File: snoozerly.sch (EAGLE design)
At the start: 55 parts, among them Q1 MOSFET_PCHANNEL, Q2 MOSFET-NCHANNELFDD8780, Q3 MOSFET-NCHANNELBSS123LT1G, Q4 MOSFET-NCHANNELBSS123LT1G, U1 ATMEGA328P, Y1 32KHz, Y2 8MHz

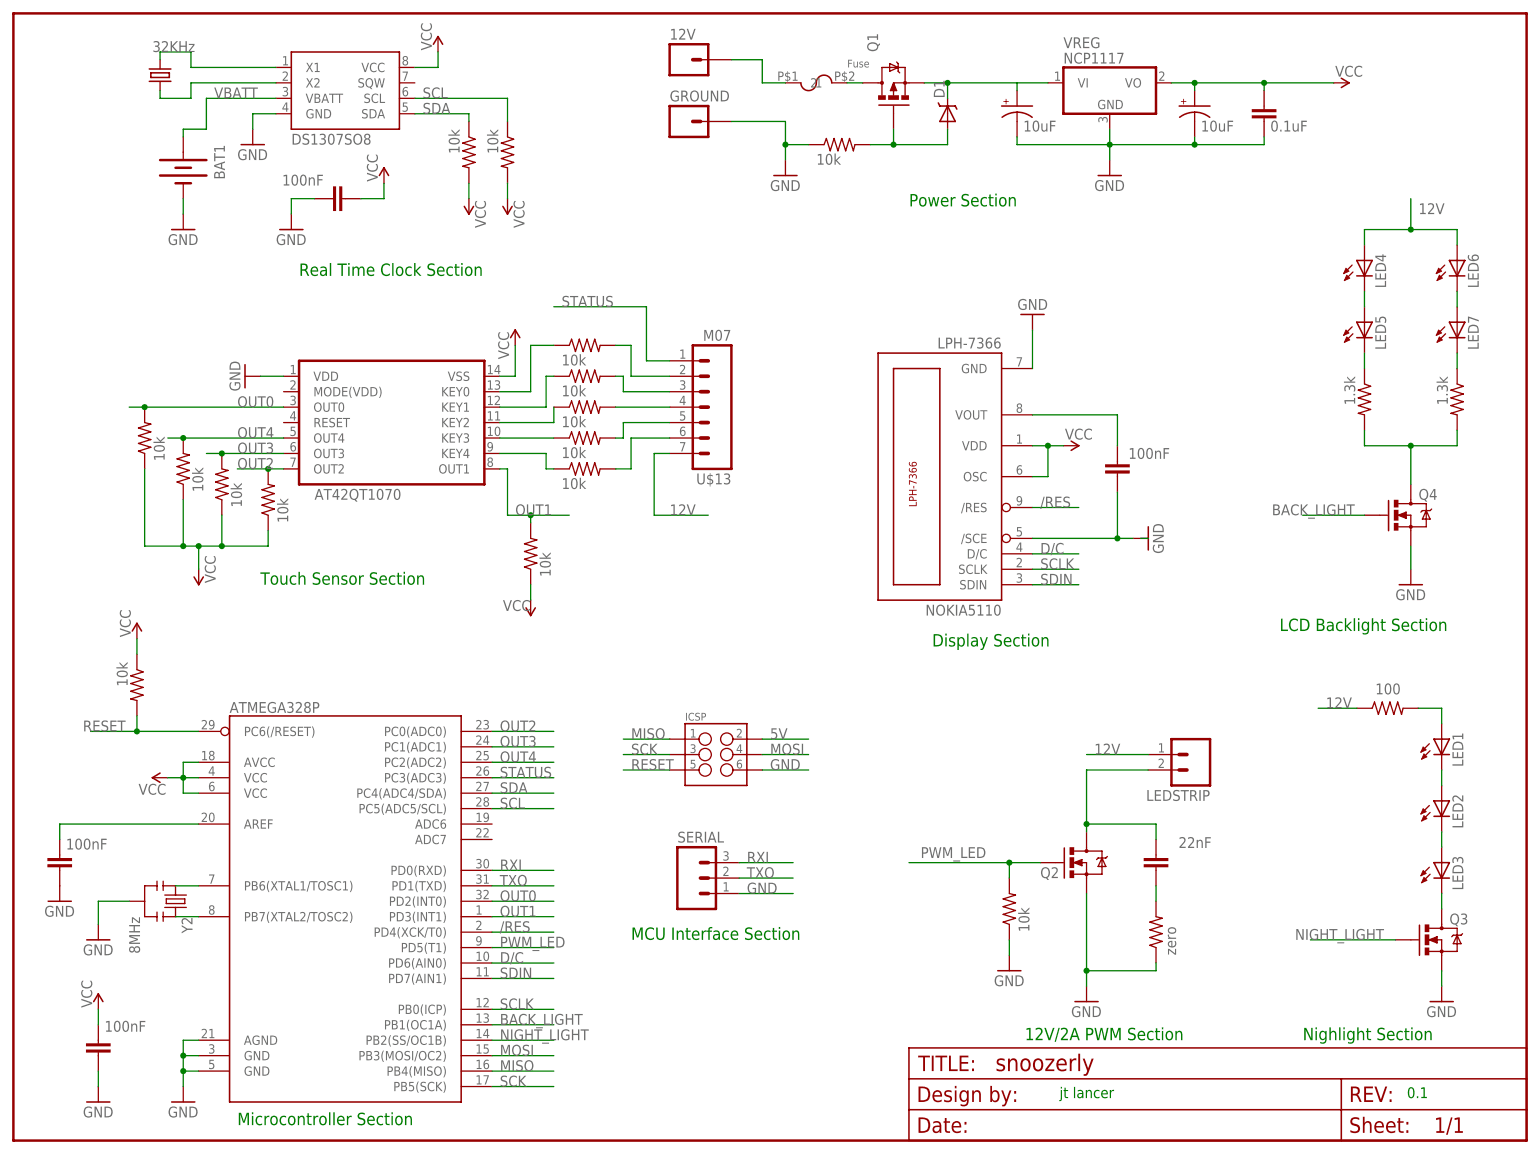
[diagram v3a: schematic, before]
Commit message: added top control board.
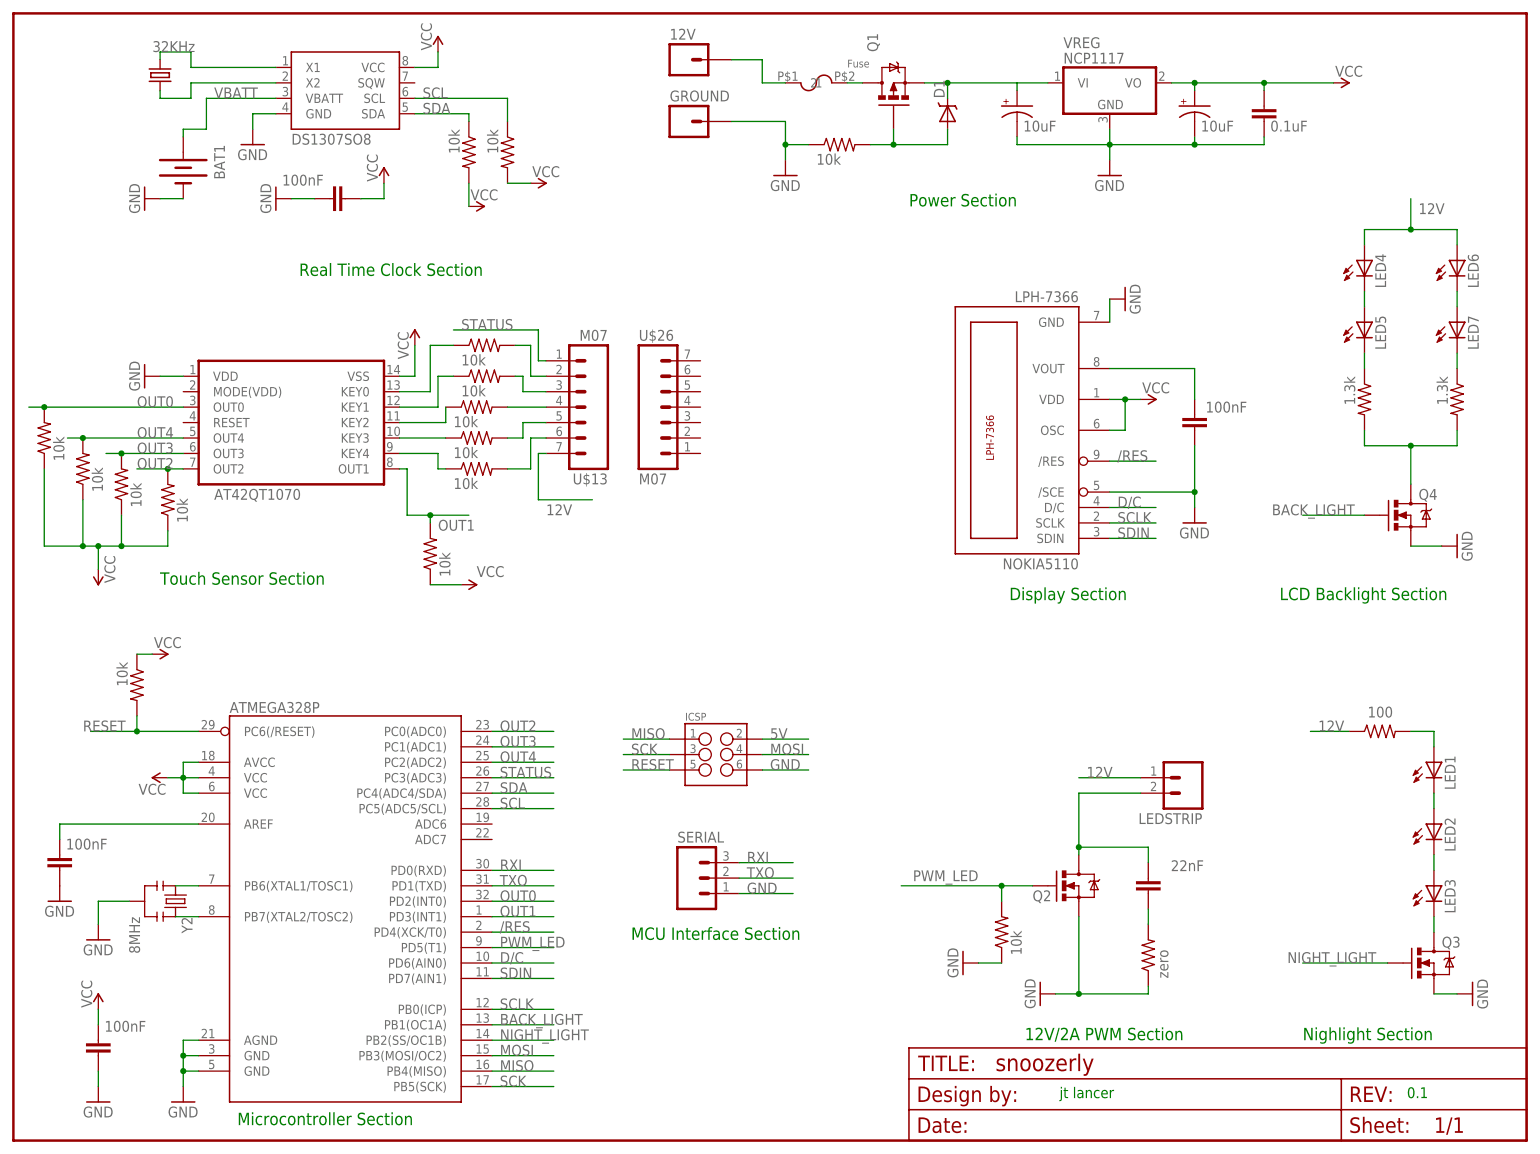
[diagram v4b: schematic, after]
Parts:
- added U$26: M07, jt_parts:M07
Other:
- moved on the sheet: LED1, LED2, LED3, LEDSTRIP, NOKIA5110, Q2, Q3, U$13

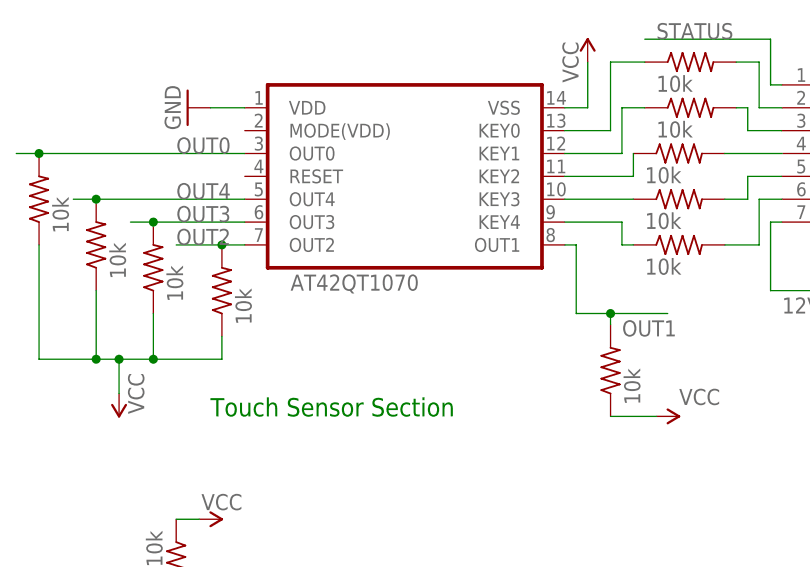
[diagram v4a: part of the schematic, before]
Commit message: updated diode and SO-14 footprint
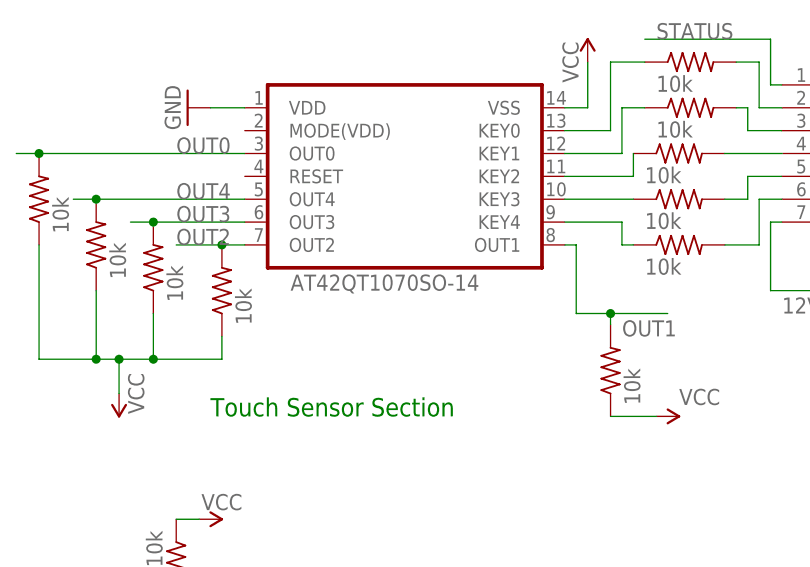
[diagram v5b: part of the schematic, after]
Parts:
- AT42QT1070: value AT42QT1070 -> AT42QT1070SO-14; device jt_parts:AT42QT1070 -> jt_parts:AT42QT1070SO-14
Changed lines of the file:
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@@
 <part name="GND1" library="SparkFun-Aesthetics" deviceset="GND" device=""/>
 <part name="U$1" library="jt_parts" deviceset="FRAME_LETTER" device=""/>
-<part name="AT42QT1070" library="jt_parts" deviceset="AT42QT1070" device=""/>
+<part name="AT42QT1070" library="jt_parts" deviceset="AT42QT1070" device="SO-14" value="AT42QT1070SO-14"/>
 <part name="SUPPLY2" library="SparkFun-Aesthetics" deviceset="VCC" device=""/>
 <part name="GND3" library="SparkFun-Aesthetics" deviceset="GND" device=""/>

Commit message: before modifying vreg footprint
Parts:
- removed U$26: M07, jt_parts:M07
- SERIAL: device SparkFun-Connectors:M03POGO_PIN_HOLES_ONLY -> SparkFun-Connectors:M031X03_NO_SILK
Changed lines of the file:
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@@
 <part name="C6" library="SparkFun-Capacitors" deviceset="CAP" device="0805" value="100nF"/>
 <part name="SUPPLY10" library="SparkFun-Aesthetics" deviceset="VCC" device=""/>
-<part name="SERIAL" library="SparkFun-Connectors" deviceset="M03" device="POGO_PIN_HOLES_ONLY"/>
+<part name="SERIAL" library="SparkFun-Connectors" deviceset="M03" device="1X03_NO_SILK"/>
 <part name="ICSP" library="SparkFun-Connectors" deviceset="M03X2" device="POGO_PINS"/>
 <part name="Q4" library="SparkFun-DiscreteSemi" deviceset="MOSFET-NCHANNEL" device="BSS123LT1G"/>
@@
 <part name="SUPPLY11" library="SparkFun-Aesthetics" deviceset="VCC" device=""/>
 <part name="U$25" library="adafruit" deviceset="R-US_" device="R0603" value="zero"/>
-<part name="U$26" library="jt_parts" deviceset="M07" device=""/>
 </parts>
 <sheets>
@@
 <attribute name="VALUE" x="205.232" y="135.89" size="1.778" layer="96" rot="R90"/>
 </instance>
-<instance part="U$26" gate="G$1" x="123.19" y="229.87"/>
 </instances>
 <busses>
@@
 </segment>
 <segment>
-<wire x1="134.62" y1="149.86" x2="143.51" y2="149.86" width="0.1524" layer="91"/>
-<pinref part="SERIAL" gate="G$1" pin="1"/>
-<label x="135.89" y="149.86" size="1.778" layer="95"/>
-</segment>
-<segment>
 <pinref part="ICSP" gate="G$1" pin="6"/>
 <wire x1="138.43" y1="170.18" x2="146.05" y2="170.18" width="0.1524" layer="91"/>
@@
 <wire x1="245.11" y1="207.01" x2="250.19" y2="207.01" width="0.1524" layer="91"/>
 </segment>
+<segment>
+<pinref part="SERIAL" gate="G$1" pin="1"/>
+<wire x1="134.62" y1="149.86" x2="143.51" y2="149.86" width="0.1524" layer="91"/>
+<label x="135.89" y="149.86" size="1.778" layer="95"/>
+</segment>
 </net>

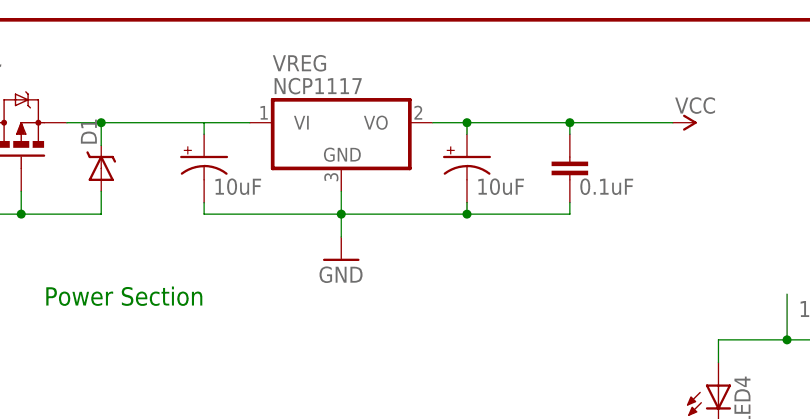
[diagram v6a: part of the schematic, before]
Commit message: updated vreg pinouts/footprint and rerouted traces
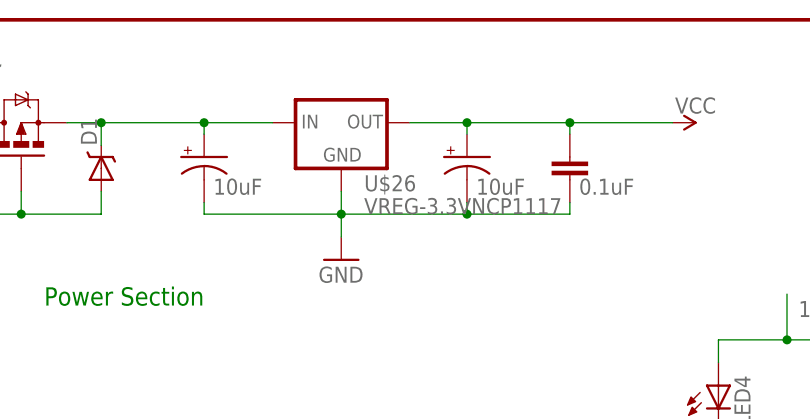
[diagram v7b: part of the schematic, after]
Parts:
- removed VREG: NCP1117, adafruit:7805DT
- added U$26: VREG-3.3VNCP1117, jt_parts:VREG-3.3VNCP1117
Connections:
- net 12V: now also U$26.IN; no longer VREG.VI
- net 5V: now also U$26.OUT; no longer VREG.VO
- net GND: now also U$26.GND; no longer VREG.GND
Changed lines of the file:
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@@
 </classes>
 <parts>
-<part name="VREG" library="adafruit" deviceset="78*" device="DT" technology="05" value="NCP1117"/>
 <part name="C8" library="SparkFun-Capacitors" deviceset="CAP" device="0805" value="0.1uF"/>
 <part name="SUPPLY3" library="SparkFun-Aesthetics" deviceset="VCC" device=""/>
@@
 <part name="SUPPLY11" library="SparkFun-Aesthetics" deviceset="VCC" device=""/>
 <part name="U$25" library="adafruit" deviceset="R-US_" device="R0603" value="zero"/>
+<part name="U$26" library="jt_parts" deviceset="VREG-3.3V" device="NCP1117"/>
 </parts>
 <sheets>
@@
 </plain>
 <instances>
-<instance part="VREG" gate="A1" x="195.58" y="283.21"/>
 <instance part="C8" gate="G$1" x="220.98" y="276.86" smashed="yes">
 <attribute name="VALUE" x="221.996" y="275.209" size="1.778" layer="96"/>
@@
 <attribute name="VALUE" x="205.232" y="135.89" size="1.778" layer="96" rot="R90"/>
 </instance>
+<instance part="U$26" gate="G$1" x="195.58" y="283.21"/>
 </instances>
 <busses>
@@
 <net name="GND" class="0">
 <segment>
-<pinref part="VREG" gate="A1" pin="GND"/>
-<wire x1="195.58" y1="275.59" x2="195.58" y2="273.05" width="0.1524" layer="91"/>
 <wire x1="195.58" y1="273.05" x2="195.58" y2="270.51" width="0.1524" layer="91"/>
 <wire x1="180.34" y1="274.32" x2="180.34" y2="273.05" width="0.1524" layer="91"/>
@@
 <wire x1="220.98" y1="273.05" x2="209.55" y2="273.05" width="0.1524" layer="91"/>
 <junction x="209.55" y="273.05"/>
+<pinref part="U$26" gate="G$1" pin="GND"/>
+<wire x1="195.58" y1="275.59" x2="195.58" y2="273.05" width="0.1524" layer="91"/>
 </segment>
 <segment>
@@
 <wire x1="220.98" y1="283.21" x2="232.41" y2="283.21" width="0.1524" layer="91"/>
 <wire x1="220.98" y1="281.94" x2="220.98" y2="283.21" width="0.1524" layer="91"/>
-<pinref part="VREG" gate="A1" pin="VO"/>
-<wire x1="205.74" y1="283.21" x2="209.55" y2="283.21" width="0.1524" layer="91"/>
 <wire x1="209.55" y1="283.21" x2="220.98" y2="283.21" width="0.1524" layer="91"/>
-<junction x="209.55" y="283.21"/>
 <pinref part="C7" gate="G$1" pin="+"/>
 <wire x1="209.55" y1="281.94" x2="209.55" y2="283.21" width="0.1524" layer="91"/>
 <junction x="220.98" y="283.21"/>
+<pinref part="U$26" gate="G$1" pin="OUT"/>
+<wire x1="203.2" y1="283.21" x2="209.55" y2="283.21" width="0.1524" layer="91"/>
+<junction x="209.55" y="283.21"/>
 </segment>
 <segment>
@@
 <wire x1="168.91" y1="283.21" x2="180.34" y2="283.21" width="0.1524" layer="91"/>
 <junction x="168.91" y="283.21"/>
-<pinref part="VREG" gate="A1" pin="VI"/>
-<wire x1="185.42" y1="283.21" x2="180.34" y2="283.21" width="0.1524" layer="91"/>
 <pinref part="C5" gate="G$1" pin="+"/>
 <wire x1="180.34" y1="281.94" x2="180.34" y2="283.21" width="0.1524" layer="91"/>
-</segment>
-<segment>
+<pinref part="U$26" gate="G$1" pin="IN"/>
+<wire x1="187.96" y1="283.21" x2="180.34" y2="283.21" width="0.1524" layer="91"/>
+<junction x="180.34" y="283.21"/>
+</segment>
+<segment>

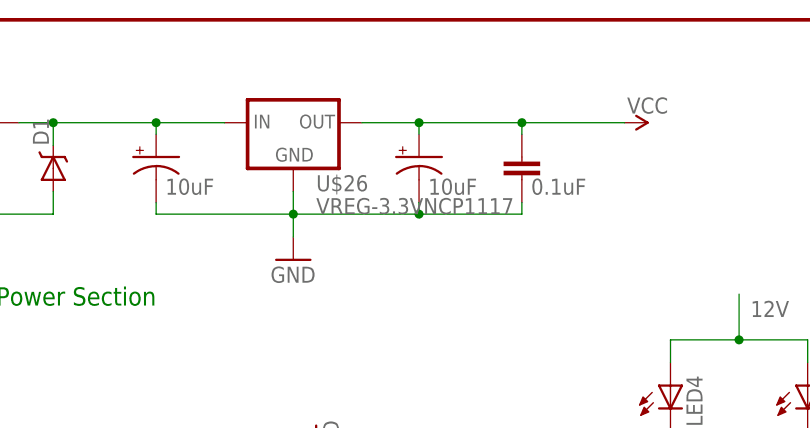
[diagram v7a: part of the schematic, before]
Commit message: update pchannel footprint and fixed spacings
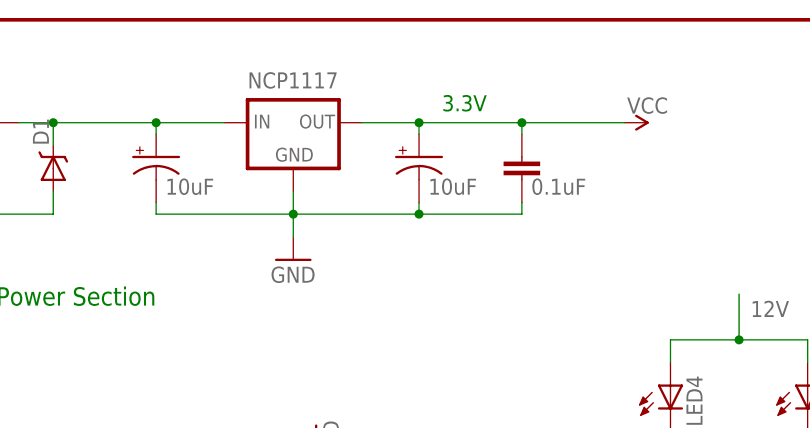
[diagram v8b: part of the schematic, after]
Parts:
- renumbered U$26 to NCP1117
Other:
- note added: "3.3V"
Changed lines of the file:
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@@
 <part name="SUPPLY11" library="SparkFun-Aesthetics" deviceset="VCC" device=""/>
 <part name="U$25" library="adafruit" deviceset="R-US_" device="R0603" value="zero"/>
-<part name="U$26" library="jt_parts" deviceset="VREG-3.3V" device="NCP1117"/>
+<part name="NCP1117" library="jt_parts" deviceset="VREG-3.3V" device="NCP1117"/>
 </parts>
 <sheets>
@@
 <text x="179.07" y="198.12" size="2.032" layer="91">Display Section</text>
 <text x="162.56" y="262.89" size="2.032" layer="91">Power Section</text>
+<text x="212.09" y="284.48" size="1.778" layer="91">3.3V</text>
 </plain>
 <instances>
@@
 <attribute name="VALUE" x="205.232" y="135.89" size="1.778" layer="96" rot="R90"/>
 </instance>
-<instance part="U$26" gate="G$1" x="195.58" y="283.21"/>
+<instance part="NCP1117" gate="G$1" x="195.58" y="283.21" smashed="yes">
+<attribute name="NAME" x="190.5" y="287.02" size="1.778" layer="95"/>
+</instance>
 </instances>
 <busses>
@@
 <wire x1="220.98" y1="273.05" x2="209.55" y2="273.05" width="0.1524" layer="91"/>
 <junction x="209.55" y="273.05"/>
-<pinref part="U$26" gate="G$1" pin="GND"/>
+<pinref part="NCP1117" gate="G$1" pin="GND"/>
 <wire x1="195.58" y1="275.59" x2="195.58" y2="273.05" width="0.1524" layer="91"/>
 </segment>
@@
 <wire x1="209.55" y1="281.94" x2="209.55" y2="283.21" width="0.1524" layer="91"/>
 <junction x="220.98" y="283.21"/>
-<pinref part="U$26" gate="G$1" pin="OUT"/>
+<pinref part="NCP1117" gate="G$1" pin="OUT"/>
 <wire x1="203.2" y1="283.21" x2="209.55" y2="283.21" width="0.1524" layer="91"/>
 <junction x="209.55" y="283.21"/>
@@
 <pinref part="C5" gate="G$1" pin="+"/>
 <wire x1="180.34" y1="281.94" x2="180.34" y2="283.21" width="0.1524" layer="91"/>
-<pinref part="U$26" gate="G$1" pin="IN"/>
+<pinref part="NCP1117" gate="G$1" pin="IN"/>
 <wire x1="187.96" y1="283.21" x2="180.34" y2="283.21" width="0.1524" layer="91"/>
 <junction x="180.34" y="283.21"/>
